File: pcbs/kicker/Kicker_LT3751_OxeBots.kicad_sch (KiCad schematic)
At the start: 121 parts, among them J1 XT30PW-F, J2 12V, J3 3.3V, J4 I2C, J5 ST Link, J6 XT30PW-F, Q1 IRFB4227, Q2 BSS138, Q3 BSS138, Q4 FQPF20N60, SW1 SW_Push, T1 DCT15EFD-U44S003, U1 STM32G031F6Px, U2 LT3751, U3 TLV9002, U4 AQV454, U5 HCNR201, U6 HCPL-3120, U7 LM358

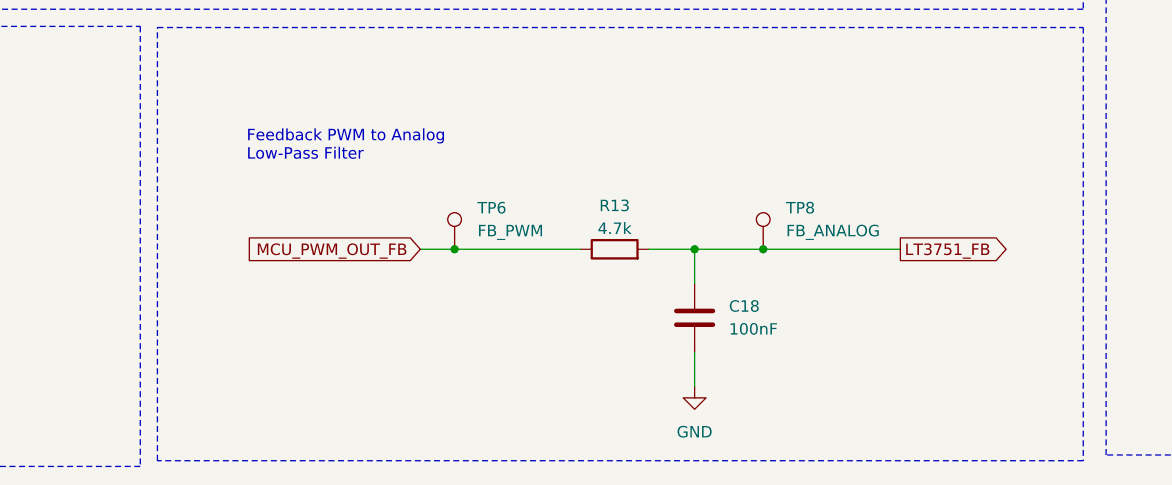
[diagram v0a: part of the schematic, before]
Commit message: Update FB low pass filter
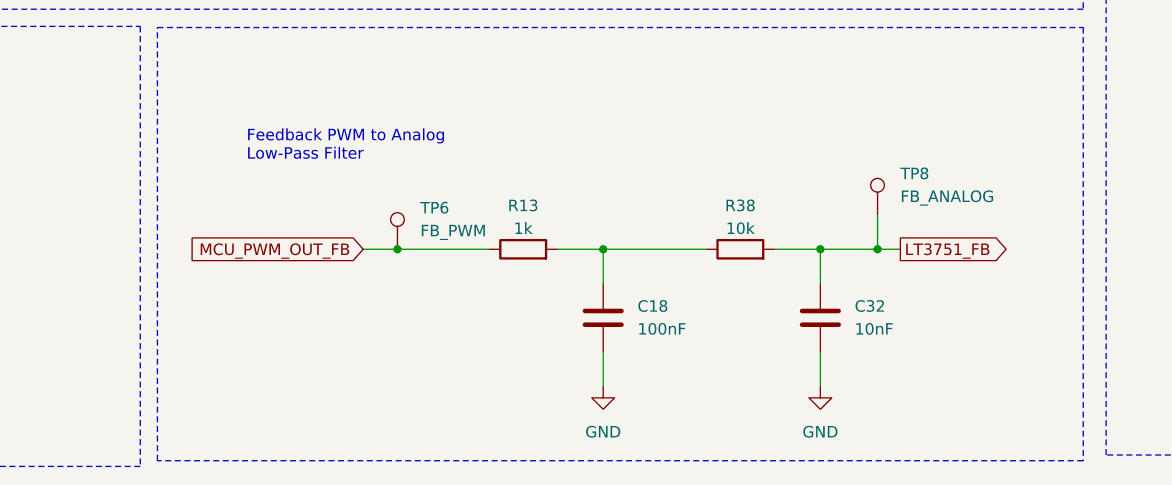
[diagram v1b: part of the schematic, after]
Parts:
- added C32: 10nF, Capacitor_SMD:C_0805_2012Metric_Pad1.18x1.45mm_HandSolder, symbol Device:C
- added R38: 10k, Resistor_SMD:R_0805_2012Metric_Pad1.20x1.40mm_HandSolder, symbol Device:R
- R13: value 4.7k -> 1k
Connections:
- net GND: now also C32.2
- net LT3751_FB: now also C32.1, R38.2; no longer C18.1, R13.2
- new net: C18.1, R13.2, R38.1
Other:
- moved on the sheet: C18, R13, TP6, TP8

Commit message: Updated to IDC Connector
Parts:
- removed J1: XT30PW-F, oxebots:AMASS_XT30PW-M, symbol oxebots:XT30PW-F
- removed J2: 12V, Connector_JST:JST_PH_S2B-PH-K_1x02_P2.00mm_Horizontal, symbol Connector_Generic:Conn_01x02
- removed J3: 3.3V, Connector_JST:JST_PH_S2B-PH-K_1x02_P2.00mm_Horizontal, symbol Connector_Generic:Conn_01x02
- removed J4: I2C, Connector_JST:JST_PH_S4B-PH-K_1x04_P2.00mm_Horizontal, symbol Connector_Generic:Conn_01x04
- added C21: 470uF, Capacitor_SMD:CP_Elec_8x10, symbol Device:C_US
- added J2: IDC_16_pin_Odd_Even, Connector_IDC:IDC-Header_2x08_P2.54mm_Vertical, symbol Connector_Generic:Conn_02x08_Odd_Even
- renumbered C5 to C1, C13 to C11, C11 to C12, C12 to C13, C17 to C15, C18 to C16, C15 to C17, C16 to C18, C32 to C20, C20 to C22, C21 to C24, C22 to C25, C25 to C26, C24 to C28, C26 to C29, C28 to C30, C30 to C31, C29 to C32, C31 to C33, C1 to C4, C4 to C5, C9 to C6, C6 to C8, C8 to C9, D2 to D1, D1 to D2, J5 to J1, J6 to J3, R13 to R11, R11 to R12, R12 to R13, R38 to R17, R17 to R18, R18 to R19, R19 to R20, R20 to R21, R21 to R22, R22 to R23, R23 to R24, R24 to R25, R25 to R26, R26 to R27, R27 to R28, R28 to R29, R29 to R31, R31 to R32, R32 to R33, R33 to R34, R34 to R35, R35 to R36, R36 to R37, R37 to R38, TP2 to TP1, TP1 to TP2
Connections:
- net +12V: now also C21.1, J2.7 (Pin_7)
- net +3.3V: now also J2.9 (Pin_9)
- net GND: now also C21.2, J2.11 (Pin_11), J2.12 (Pin_12), J2.13 (Pin_13), J2.14 (Pin_14), J2.15 (Pin_15), J2.16 (Pin_16)
- net MCU_I2C_SCL: now also J2.10 (Pin_10)
- net MCU_I2C_SDA: now also J2.8 (Pin_8)
- net +24V_INPUT: now reaches F1.1
- net +24V_INPUT: now also J2.1 (Pin_1), J2.2 (Pin_2), J2.3 (Pin_3), J2.4 (Pin_4), J2.5 (Pin_5), J2.6 (Pin_6)
- net MCU_OUT_ENABLE renamed MCU_OUT_CHARGE
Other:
- note added: "GND"
- note added: "IDC Interface"
- note removed: "External Interface I2C"
- moved on the sheet: C1, C11, C12, C13, C15, C16, C17, C18, C2, C20, C28, C3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

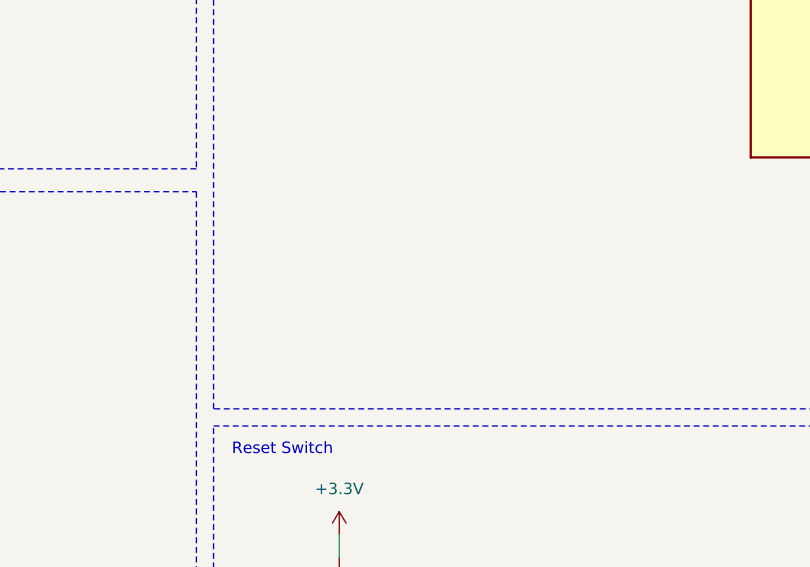
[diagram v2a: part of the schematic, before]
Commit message: added I2C pull-up resistors
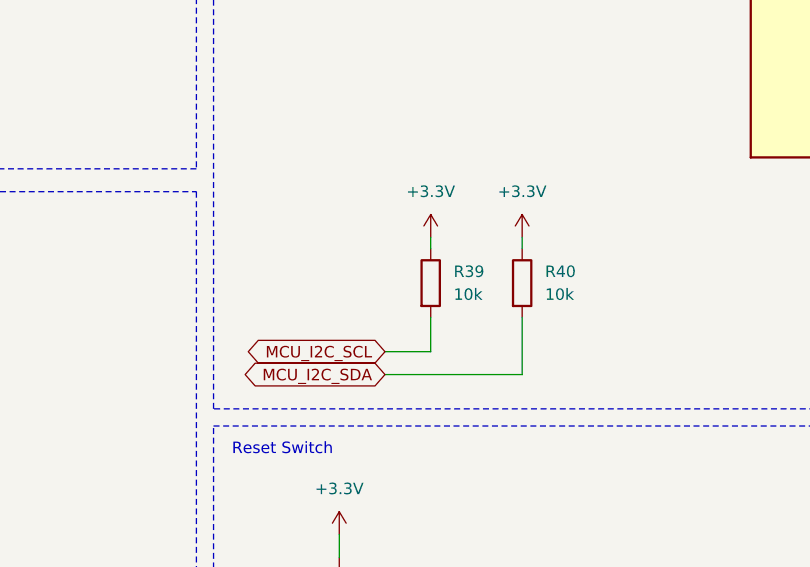
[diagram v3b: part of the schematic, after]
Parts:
- added R39, R40: 10k, Resistor_SMD:R_0805_2012Metric_Pad1.20x1.40mm_HandSolder, symbol Device:R
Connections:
- net +3.3V: now also R39.1, R40.1
- net MCU_I2C_SCL: now also R39.2
- net MCU_I2C_SDA: now also R40.2
